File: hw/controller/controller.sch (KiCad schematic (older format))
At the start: 72 parts, among them J1 ARM-SWD, J2 USB_OTG, J3 UART, P1 TH0, P14 I2C0, P15 I2C1, P16 I2C2, P17 I2C3, P2 FRIDGE, P3 FAN, P4 PUMP, P5 MIST, P6 TH1, P7 TH2, P8 TH3, SW1 RST, SW2 BOOT, U1 stm32f072x, U2 MIC550X, U3 tca9546a, U4 SHT3x-DIS, U5 SHT3x-DIS, U6 SHT3x-DIS, U7 SHT3x-DIS, U8 SHT3x-DIS, Y2 32768Hz

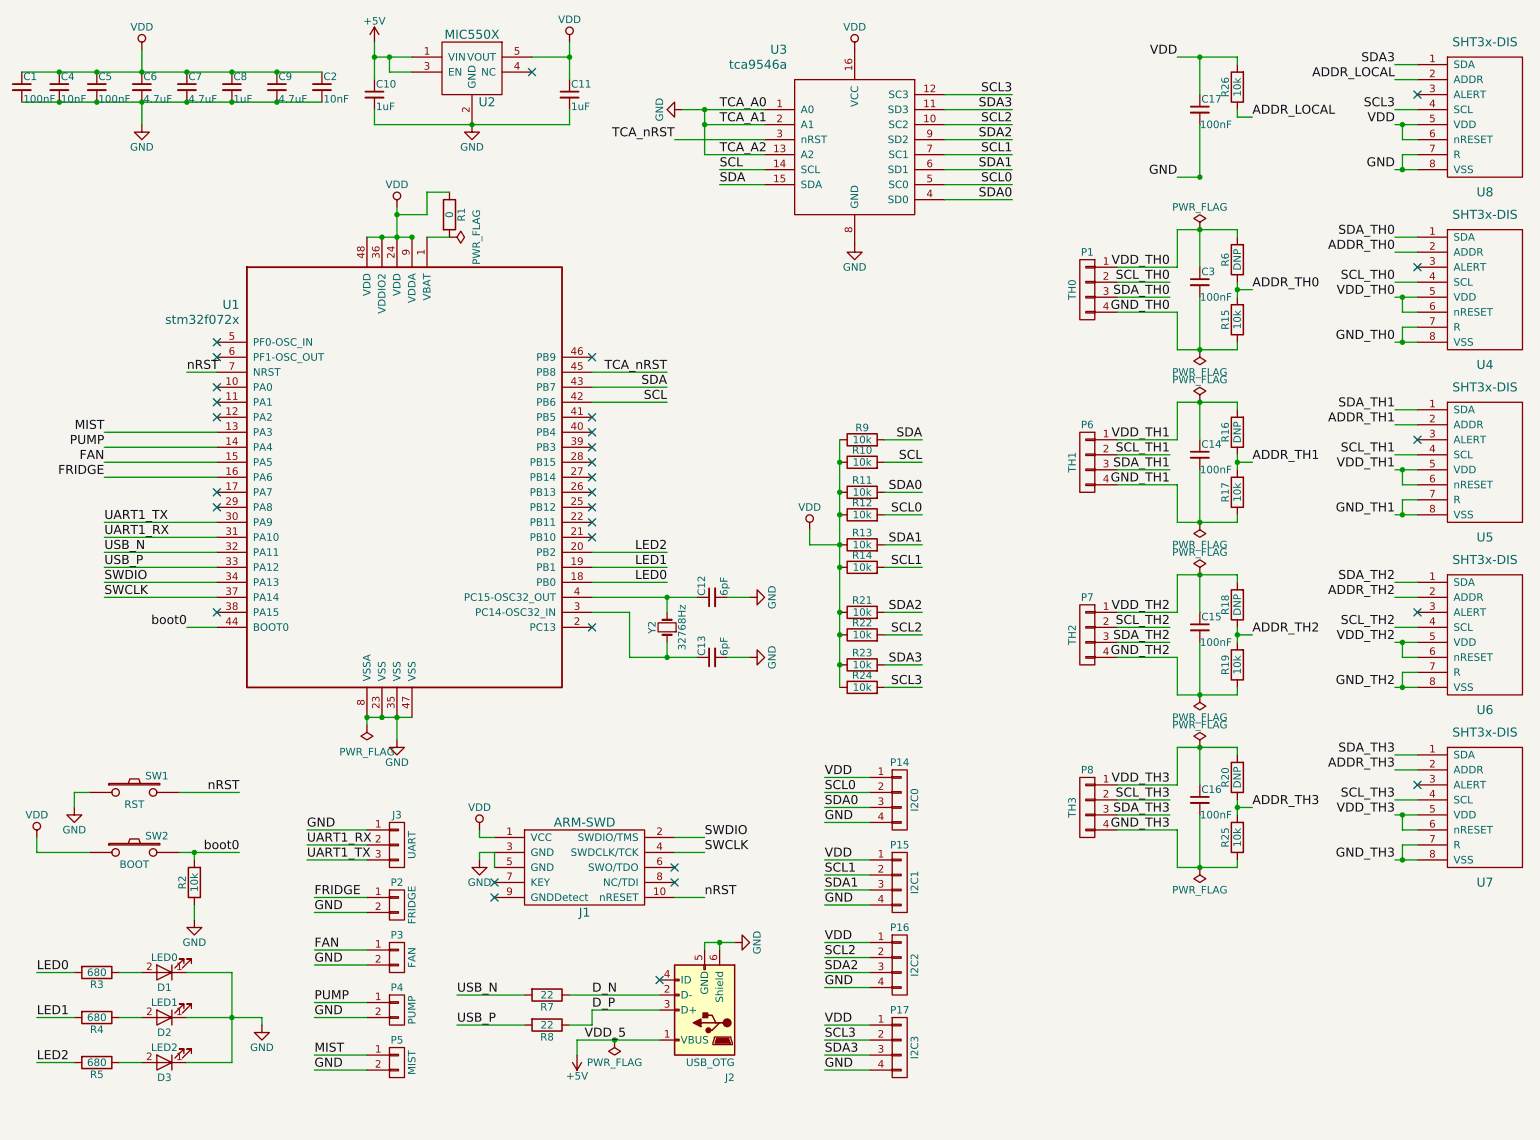
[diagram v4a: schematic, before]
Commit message: Removed sensor breakouts from controller
Updated silkscreen
Removed SWD connector
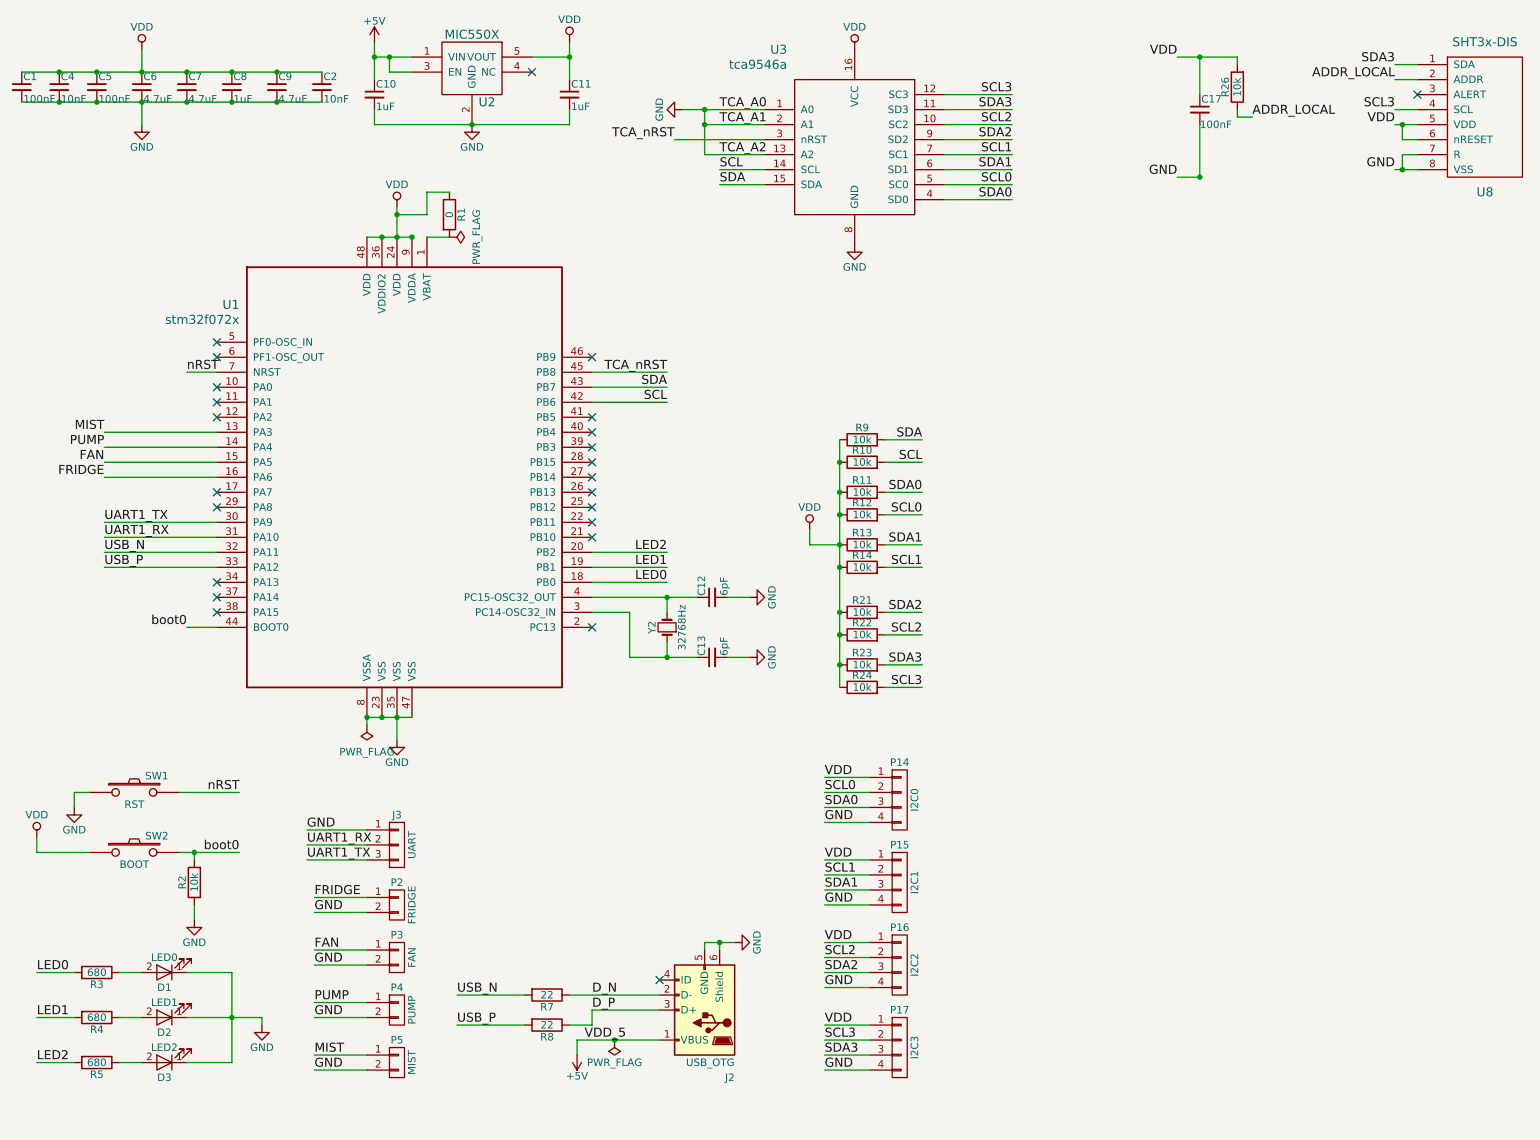
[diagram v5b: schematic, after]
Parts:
- removed C14, C15, C16, C3: 100nF, Capacitors_SMD:C_0603, symbol C_Small
- removed J1: ARM-SWD, footprints:ARM_SWD_SMD, symbol ARM-SWD
- removed P1: TH0, Pin_Headers:Pin_Header_Straight_1x04_Pitch2.54mm, symbol CONN_01X04
- removed P6: TH1, Pin_Headers:Pin_Header_Straight_1x04_Pitch2.54mm, symbol CONN_01X04
- removed P7: TH2, Pin_Headers:Pin_Header_Straight_1x04_Pitch2.54mm, symbol CONN_01X04
- removed P8: TH3, Pin_Headers:Pin_Header_Straight_1x04_Pitch2.54mm, symbol CONN_01X04
- removed R15, R17, R19, R25: 10k, Resistors_SMD:R_0603, symbol R
- removed R16, R18, R20, R6: DNP, Resistors_SMD:R_0603, symbol R
- removed U4, U5, U6, U7: SHT3x-DIS, footprints:SHT3x, symbol SHT3x-DIS
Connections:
- net SWCLK: no longer names the net of U1.37 (PA14)
- net SWDIO: no longer names the net of U1.34 (PA13)
- no-connect marks 30 -> 24

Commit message: Updated ostur_controller with NRF52810. Released v2.0
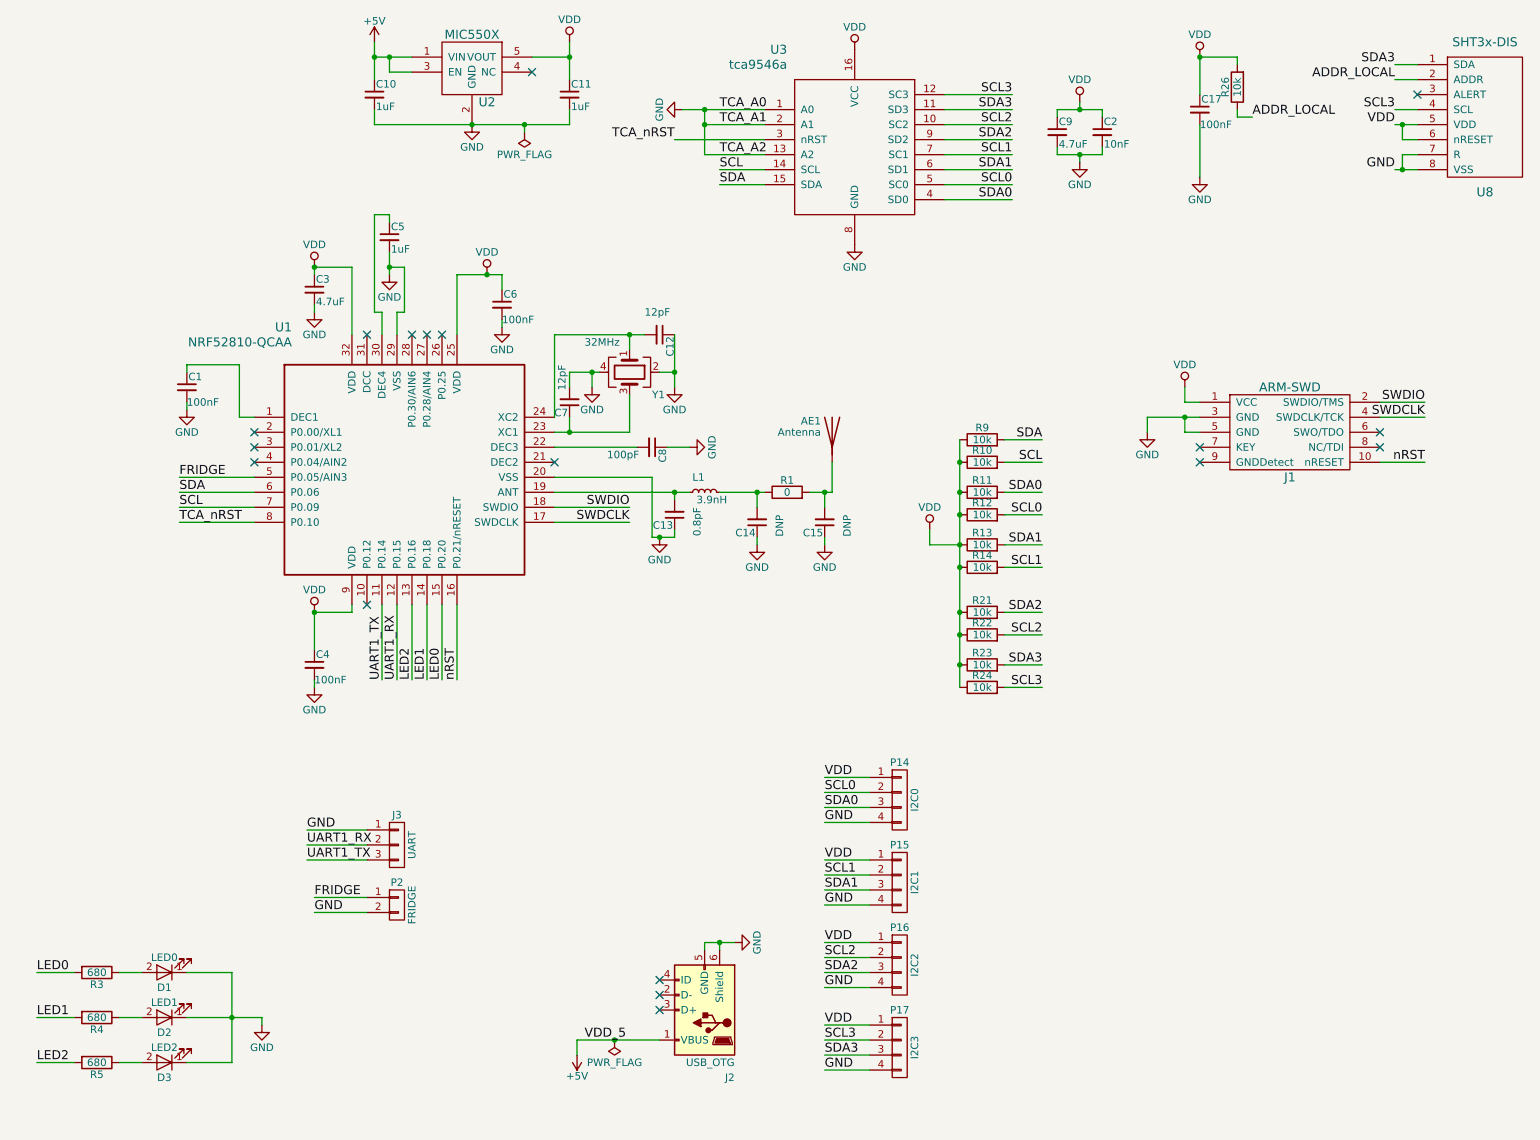
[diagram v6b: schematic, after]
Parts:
- removed P3: FAN, Pin_Headers:Pin_Header_Straight_1x02_Pitch2.54mm, symbol CONN_01X02
- removed P4: PUMP, Pin_Headers:Pin_Header_Straight_1x02_Pitch2.54mm, symbol CONN_01X02
- removed P5: MIST, Pin_Headers:Pin_Header_Straight_1x02_Pitch2.54mm, symbol CONN_01X02
- removed R2: 10k, Resistors_SMD:R_0603, symbol R
- removed R7, R8: 22, Resistors_SMD:R_0603, symbol R
- removed SW1: RST, footprints:PTS645SM43SMTR92, symbol SW_PUSH
- removed SW2: BOOT, footprints:PTS645SM43SMTR92, symbol SW_PUSH
- removed U1: stm32f072x, footprints:LQFP48, symbol stm32f072x
- removed Y2: 32768Hz, footprints:FC-135, symbol Crystal_Small
- added AE1: Antenna, alvarop:AMCA31-2R450G-S1F-T3, symbol Antenna
- added C14, C15: DNP, Capacitors_SMD:C_0603, symbol C_Small
- added C3: 4.7uF, Capacitors_SMD:C_0603, symbol C_Small
- added J1: ARM-SWD, alvarop:ARM_SWD_SMD, symbol ARM-SWD
- added L1: 3.9nH, Resistors_SMD:R_0603, symbol L_Small
- added U1: NRF52810-QCAA, alvarop:NRF52810_QCAA_QFN32, symbol NRF52810-QCAA
- added Y1: 32MHz, Crystals:Crystal_SMD_2016-4pin_2.0x1.6mm, symbol Crystal_GND24
- C12: value 6pF -> 12pF; MPN CL10C060CB8NCNC -> (none)
- C13: value 6pF -> 0.8pF; MPN CL10C060CB8NCNC -> (none)
- C4: value 10nF -> 100nF; MPN CL21B103KBANNNC -> CL21B104MBCNNNC
- C5: value 100nF -> 1uF; MPN CL21B104MBCNNNC -> CL21F105ZAFNNNG
- C6: value 4.7uF -> 100nF; MPN CL21A475KQFNNNG -> CL21B104MBCNNNC
- C7: value 4.7uF -> 12pF; MPN CL21A475KQFNNNG -> (none)
- C8: value 1uF -> 100pF; MPN CL21F105ZAFNNNG -> (none)
- R1: MPN MCR10ERTJ000 -> (none)
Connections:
- net FRIDGE: now also U1.5 (P0.05/AIN3)
- net GND: now also C12.1, C13.1, C8.1, C14.1, C15.1, C3.2, J1.3 (GND), J1.5 (GND), U1.20 (VSS), U1.29 (VSS), Y1.2, Y1.4; no longer C12.2, C13.2, C8.2
- net LED0: now also U1.15 (P0.20)
- net LED1: now also U1.14 (P0.18)
- net LED2: now also U1.13 (P0.16)
- net SCL: now also U1.7 (P0.09)
- net SDA: now also U1.6 (P0.06)
- net TCA_nRST: now also U1.8 (P0.10)
- net UART1_RX: now also U1.12 (P0.15)
- net UART1_TX: now also U1.11 (P0.14)
- net VDD: now also C3.1, J1.1 (VCC), U1.25 (VDD), U1.32 (VDD), U1.9 (VDD); no longer C1.1, C5.1, C7.1, C8.1, R1.1
- net nRST: now also J1.10 (nRESET), U1.16 (P0.21/nRESET)
- net at R1.2: now also AE1.1 (A), C15.2
- net D_N: no longer names the net of J2.2 (D-)
- net D_P: no longer names the net of J2.3 (D+)
- new net: C1.1, U1.1 (DEC1)
- new net: C13.2, L1.1, U1.19 (ANT)
- new net: C8.2, U1.22 (DEC3)
- new net: C7.1, U1.23 (XC1), Y1.3
- new net: C12.2, U1.24 (XC2), Y1.1
- new net: C5.1, U1.30 (DEC4)
- new net: C14.2, L1.2, R1.1
- new net SWDCLK: J1.4 (SWDCLK/TCK), U1.17 (SWDCLK)
- new net SWDIO: J1.2 (SWDIO/TMS), U1.18 (SWDIO)
- no-connect marks 24 -> 18
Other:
- moved on the sheet: C2, C9, R10, R11, R12, R13, R14, R21, R22, R23, R24, R9

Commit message: Released Ostur Controller v2.1
NOTE: Used kicad 5
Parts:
- removed J3: UART, Pin_Headers:Pin_Header_Straight_1x03_Pitch1.27mm, symbol CONN_01X03
- added C16: 100nF, Capacitor_SMD:C_0603_1608Metric, symbol controller-rescue:C_Small
- added C18: 10nF, Capacitor_SMD:C_0603_1608Metric, symbol controller-rescue:C_Small
- added L2: FB, Resistor_SMD:R_0603_1608Metric, symbol Device:Ferrite_Bead_Small
- added R2, R6: 27, Resistor_SMD:R_0603_1608Metric, symbol controller-rescue:R
- added U4: FT234XD, alvarop:FTDI_DFN12, symbol alvarop:FT234XD
- AE1: symbol Antenna -> controller-rescue:Antenna
- C1, C10, C11, C12, C13, C14, C15, C17, C2, C3, C4, C5, C6, C7, C8, C9: footprint Capacitors_SMD:C_0603 -> Capacitor_SMD:C_0603_1608Metric; symbol C_Small -> controller-rescue:C_Small
- D1, D2, D3: symbol LED-RESCUE-controller-RESCUE-controller -> controller-rescue:LED-RESCUE-controller-RESCUE-controller
- J1: symbol ARM-SWD -> ostur:ARM-SWD
- J2: symbol USB_OTG -> controller-rescue:USB_OTG
- L1: footprint Resistors_SMD:R_0603 -> Resistor_SMD:R_0603_1608Metric; symbol L_Small -> controller-rescue:L_Small
- P14, P15, P16, P17: symbol CONN_01X04 -> controller-rescue:CONN_01X04
- P2: symbol CONN_01X02 -> controller-rescue:CONN_01X02
- R1, R10, R11, R12, R13, R14, R21, R22, R23, R24, R26, R3, R4, R5, R9: footprint Resistors_SMD:R_0603 -> Resistor_SMD:R_0603_1608Metric; symbol R -> controller-rescue:R
- U1: symbol NRF52810-QCAA -> alvarop:NRF52810-QCAA
- U2: symbol MIC550X -> ostur:MIC550X
- U3: symbol tca9546a -> ostur:tca9546a
- U8: symbol SHT3x-DIS -> ostur:SHT3x-DIS
- Y1: symbol Crystal_GND24 -> controller-rescue:Crystal_GND24
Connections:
- net labels added: USB_DM, USB_DP
- wire segments 172 -> 226
- no-connect marks 18 -> 20
